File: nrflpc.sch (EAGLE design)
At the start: 68 parts, among them IC1 LPC1111/12/13/14-HVQFN33, IC2 LT1763CS8-3.3, IC3 LM3401, IC5 LM3401, IC6 LM3401, IC7 LM3401, Q1 20MHz, Q2 MOSFET-PCHANNEL, Q3 MOSFET-PCHANNEL, Q4 MOSFET-PCHANNEL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

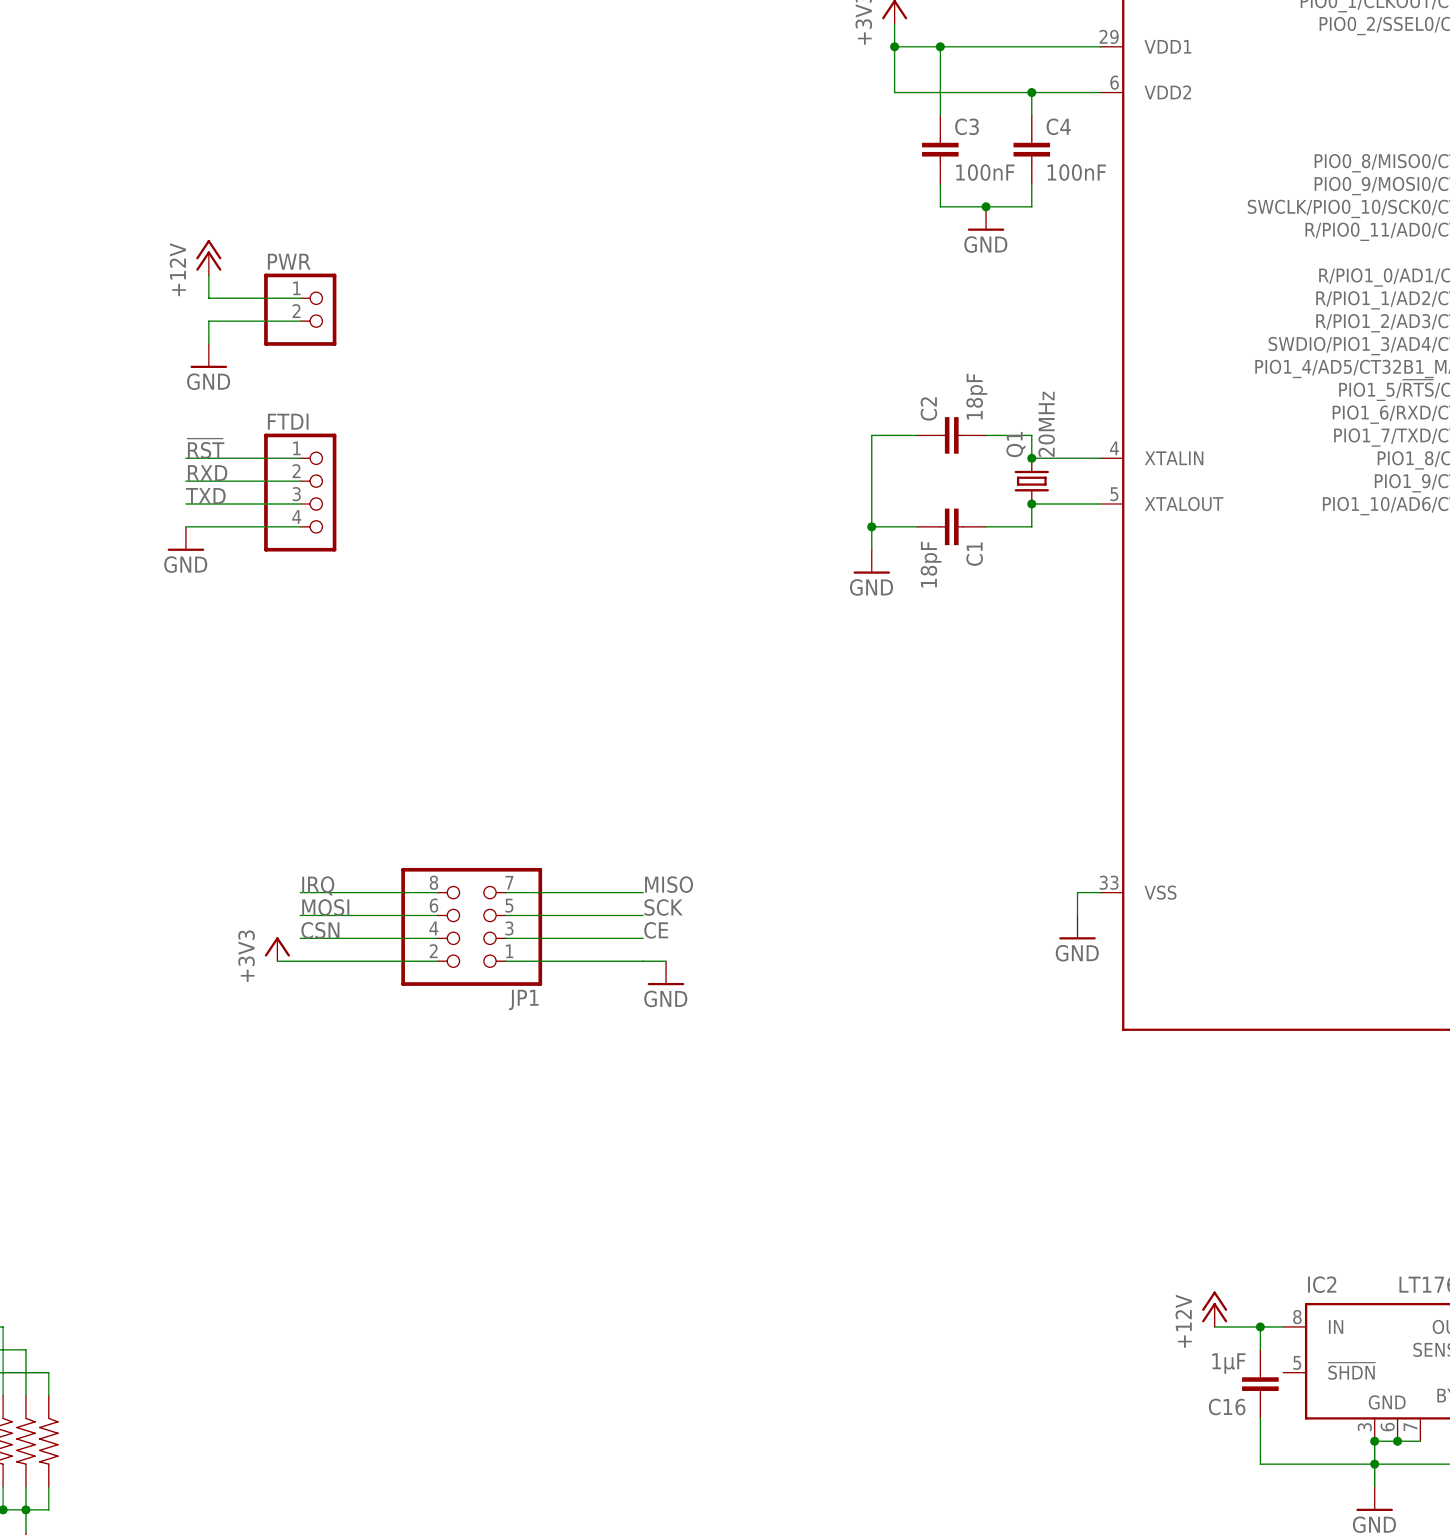
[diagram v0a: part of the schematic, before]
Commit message: Routing Voltage and "left" side (ISP)
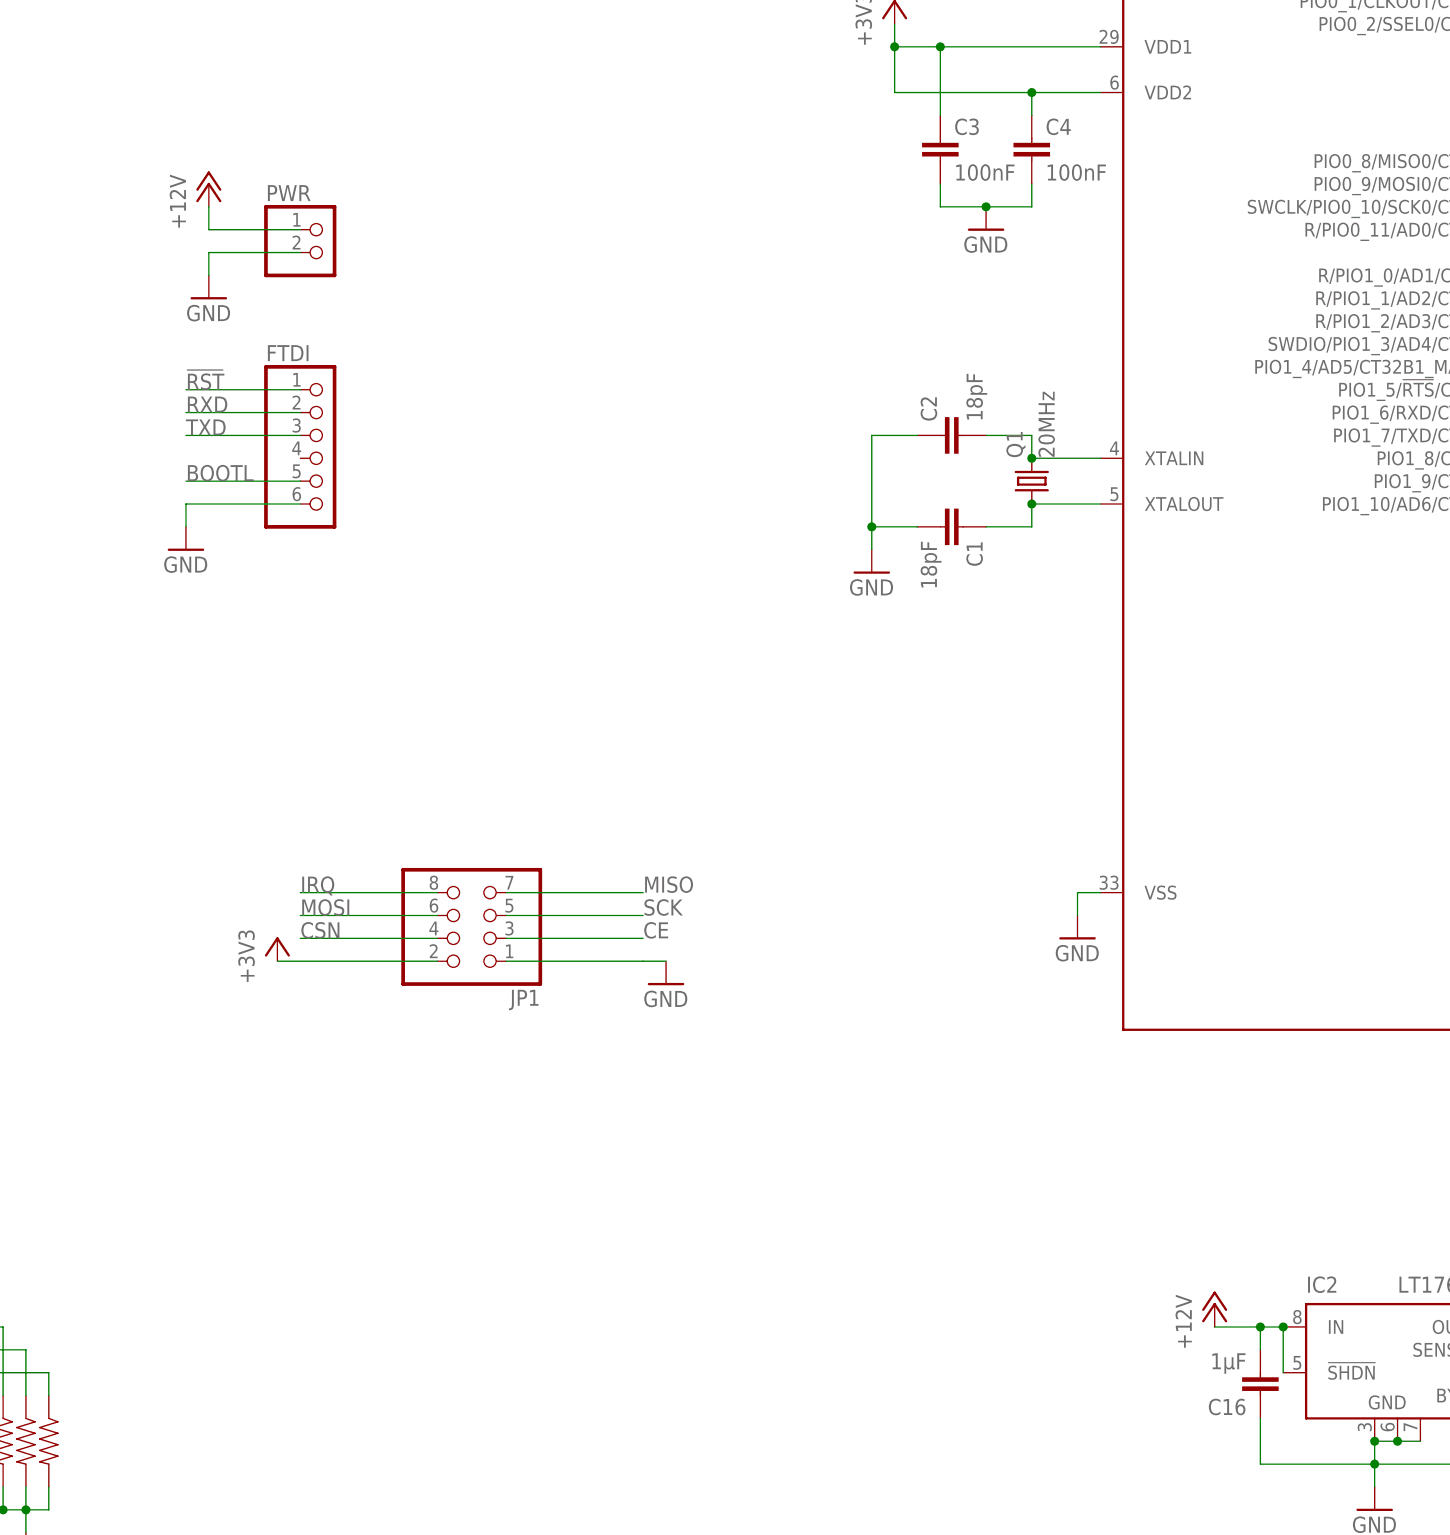
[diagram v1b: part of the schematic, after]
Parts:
- FTDI: device pinhead:PINHD-1X4 -> pinhead:PINHD-1X6
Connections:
- net +12V: now also IC2.!SHDN
- net BOOTL: now also FTDI.5
- net GND: now also FTDI.6; no longer FTDI.4
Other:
- moved on the sheet: PWR
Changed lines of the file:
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@@
 <part name="C16" library="SparkFun" deviceset="CAP" device="0805" value="1µF"/>
 <part name="+3V1" library="supply1" deviceset="+3V3" device=""/>
-<part name="FTDI" library="pinhead" deviceset="PINHD-1X4" device=""/>
+<part name="FTDI" library="pinhead" deviceset="PINHD-1X6" device=""/>
 <part name="GND8" library="supply1" deviceset="GND" device=""/>
 <part name="JP1" library="pinhead" deviceset="PINHD-2X4" device=""/>
@@
 <instance part="C16" gate="G$1" x="193.04" y="43.18" rot="R180"/>
 <instance part="+3V1" gate="G$1" x="243.84" y="50.8"/>
-<instance part="FTDI" gate="A" x="88.9" y="139.7"/>
+<instance part="FTDI" gate="A" x="88.9" y="144.78"/>
 <instance part="GND8" gate="1" x="73.66" y="134.62"/>
 <instance part="JP1" gate="A" x="106.68" y="93.98" rot="R180"/>
@@
 <instance part="GND13" gate="1" x="302.26" y="134.62"/>
 <instance part="C5" gate="G$1" x="302.26" y="144.78"/>
-<instance part="PWR" gate="G$1" x="88.9" y="160.02"/>
-<instance part="P+1" gate="1" x="76.2" y="167.64"/>
-<instance part="GND12" gate="1" x="76.2" y="154.94"/>
+<instance part="PWR" gate="G$1" x="88.9" y="167.64"/>
+<instance part="P+1" gate="1" x="76.2" y="175.26"/>
+<instance part="GND12" gate="1" x="76.2" y="162.56"/>
 <instance part="C12" gate="G$1" x="312.42" y="101.6" rot="R180"/>
 <instance part="R18" gate="G$1" x="322.58" y="109.22" rot="R180"/>
@@
 </segment>
 <segment>
-<pinref part="FTDI" gate="A" pin="4"/>
-<wire x1="86.36" y1="137.16" x2="73.66" y2="137.16" width="0.1524" layer="91"/>
-<pinref part="GND8" gate="1" pin="GND"/>
-</segment>
-<segment>
 <pinref part="JP1" gate="A" pin="1"/>
 <wire x1="109.22" y1="88.9" x2="124.46" y2="88.9" width="0.1524" layer="91"/>
@@
 <segment>
 <pinref part="PWR" gate="G$1" pin="2"/>
-<wire x1="86.36" y1="160.02" x2="76.2" y2="160.02" width="0.1524" layer="91"/>
-<wire x1="76.2" y1="160.02" x2="76.2" y2="157.48" width="0.1524" layer="91"/>
+<wire x1="86.36" y1="167.64" x2="76.2" y2="167.64" width="0.1524" layer="91"/>
+<wire x1="76.2" y1="167.64" x2="76.2" y2="165.1" width="0.1524" layer="91"/>
 <pinref part="GND12" gate="1" pin="GND"/>
 </segment>
@@
 <pinref part="GND15" gate="1" pin="GND"/>
 </segment>
+<segment>
+<pinref part="FTDI" gate="A" pin="6"/>
+<pinref part="GND8" gate="1" pin="GND"/>
+<wire x1="86.36" y1="139.7" x2="73.66" y2="139.7" width="0.1524" layer="91"/>
+<wire x1="73.66" y1="139.7" x2="73.66" y2="137.16" width="0.1524" layer="91"/>
+</segment>
 </net>
 <net name="!RST" class="0">
-<segment>
-<pinref part="FTDI" gate="A" pin="1"/>
-<wire x1="86.36" y1="144.78" x2="76.2" y2="144.78" width="0.1524" layer="91"/>
-<wire x1="76.2" y1="144.78" x2="73.66" y2="144.78" width="0.1524" layer="91"/>
-<label x="73.66" y="144.78" size="1.778" layer="95"/>
-</segment>
 <segment>
 <pinref part="C5" gate="G$1" pin="1"/>
@@
 <label x="236.22" y="198.12" size="1.778" layer="95"/>
 </segment>
+<segment>
+<pinref part="FTDI" gate="A" pin="1"/>
+<wire x1="86.36" y1="152.4" x2="73.66" y2="152.4" width="0.1524" layer="91"/>
+<label x="73.66" y="152.4" size="1.778" layer="95"/>
+</segment>
 </net>
 <net name="TXD" class="0">
-<segment>
-<pinref part="FTDI" gate="A" pin="3"/>
-<wire x1="86.36" y1="139.7" x2="73.66" y2="139.7" width="0.1524" layer="91"/>
-<label x="73.66" y="139.7" size="1.778" layer="95"/>
-</segment>
 <segment>
 <pinref part="R21" gate="G$1" pin="2"/>
@@
 <label x="248.92" y="147.32" size="1.778" layer="95"/>
 </segment>
+<segment>
+<pinref part="FTDI" gate="A" pin="3"/>
+<wire x1="86.36" y1="147.32" x2="73.66" y2="147.32" width="0.1524" layer="91"/>
+<label x="73.66" y="147.32" size="1.778" layer="95"/>
+</segment>
 </net>
 <net name="RXD" class="0">
-<segment>
-<pinref part="FTDI" gate="A" pin="2"/>
-<wire x1="86.36" y1="142.24" x2="73.66" y2="142.24" width="0.1524" layer="91"/>
-<label x="73.66" y="142.24" size="1.778" layer="95"/>
-</segment>
 <segment>
 <pinref part="R20" gate="G$1" pin="2"/>
 <wire x1="243.84" y1="149.86" x2="254" y2="149.86" width="0.1524" layer="91"/>
 <label x="248.92" y="149.86" size="1.778" layer="95"/>
+</segment>
+<segment>
+<pinref part="FTDI" gate="A" pin="2"/>
+<wire x1="86.36" y1="149.86" x2="73.66" y2="149.86" width="0.1524" layer="91"/>
+<label x="73.66" y="149.86" size="1.778" layer="95"/>
 </segment>
 </net>
@@
 <segment>
 <pinref part="PWR" gate="G$1" pin="1"/>
-<wire x1="86.36" y1="162.56" x2="76.2" y2="162.56" width="0.1524" layer="91"/>
-<wire x1="76.2" y1="162.56" x2="76.2" y2="165.1" width="0.1524" layer="91"/>
+<wire x1="86.36" y1="170.18" x2="76.2" y2="170.18" width="0.1524" layer="91"/>
+<wire x1="76.2" y1="170.18" x2="76.2" y2="172.72" width="0.1524" layer="91"/>
 <pinref part="P+1" gate="1" pin="+12V"/>
 </segment>
@@
 <wire x1="193.04" y1="45.72" x2="193.04" y2="48.26" width="0.1524" layer="91"/>
 <junction x="193.04" y="48.26"/>
+<pinref part="IC2" gate="G$1" pin="!SHDN"/>
+<wire x1="195.58" y1="43.18" x2="195.58" y2="48.26" width="0.1524" layer="91"/>
+<junction x="195.58" y="48.26"/>
 </segment>
 </net>
@@
 <wire x1="231.14" y1="195.58" x2="241.3" y2="195.58" width="0.1524" layer="91"/>
 </segment>
-</net>
+<segment>
+<pinref part="FTDI" gate="A" pin="5"/>
+<wire x1="86.36" y1="142.24" x2="73.66" y2="142.24" width="0.1524" layer="91"/>
+<label x="73.66" y="142.24" size="1.778" layer="95"/>
+</segment>
+</net>

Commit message: Almost final routing
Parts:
- added EXT: (no value), pinhead:PINHD-1X7
- added R1, R22: 1k, rcl:R-US_R0402
- added R23, R24, R25: 150, rcl:R-US_R0402
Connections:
- new net N$34: IC1.PIO0_3, R23.1
- new net N$35: IC1.PIO0_4/SCL, R24.1
- new net N$36: IC1.PIO0_5/SDA, R25.1
- net +3V3: now also EXT.6, R1.1, R22.1
- net AIN0: now also EXT.1, R1.2
- net AIN1: now also EXT.2, R22.2
- net GND: now also EXT.7
- net IO0: now also EXT.5, R23.2; no longer IC1.PIO0_3
- net IO1: now also EXT.4, R24.2; no longer IC1.PIO0_4/SCL
- net IO2: now also EXT.3, R25.2; no longer IC1.PIO0_5/SDA
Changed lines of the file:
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@@
 <part name="C18" library="SparkFun" deviceset="CAP" device="0402-CAP" value="10nF"/>
 <part name="C17" library="rcl" deviceset="CPOL-EU" device="SMCA" value="10µF"/>
+<part name="EXT" library="pinhead" deviceset="PINHD-1X7" device=""/>
+<part name="GND16" library="supply1" deviceset="GND" device=""/>
+<part name="+3V3" library="supply1" deviceset="+3V3" device=""/>
+<part name="R1" library="rcl" deviceset="R-US_" device="R0402" value="1k"/>
+<part name="R22" library="rcl" deviceset="R-US_" device="R0402" value="1k"/>
+<part name="+3V5" library="supply1" deviceset="+3V3" device=""/>
+<part name="+3V6" library="supply1" deviceset="+3V3" device=""/>
+<part name="R23" library="rcl" deviceset="R-US_" device="R0402" value="150"/>
+<part name="R24" library="rcl" deviceset="R-US_" device="R0402" value="150"/>
+<part name="R25" library="rcl" deviceset="R-US_" device="R0402" value="150"/>
 </parts>
 <sheets>
@@
 <instance part="C18" gate="G$1" x="228.6" y="43.18" rot="R180"/>
 <instance part="C17" gate="G$1" x="238.76" y="43.18"/>
+<instance part="EXT" gate="A" x="302.26" y="177.8"/>
+<instance part="GND16" gate="1" x="281.94" y="167.64"/>
+<instance part="+3V3" gate="G$1" x="281.94" y="175.26"/>
+<instance part="R1" gate="G$1" x="284.48" y="193.04" rot="R270"/>
+<instance part="R22" gate="G$1" x="276.86" y="193.04" rot="R270"/>
+<instance part="+3V5" gate="G$1" x="276.86" y="203.2"/>
+<instance part="+3V6" gate="G$1" x="284.48" y="203.2"/>
+<instance part="R23" gate="G$1" x="246.38" y="190.5"/>
+<instance part="R24" gate="G$1" x="246.38" y="187.96"/>
+<instance part="R25" gate="G$1" x="246.38" y="185.42"/>
 </instances>
 <busses>
@@
 <wire x1="73.66" y1="139.7" x2="73.66" y2="137.16" width="0.1524" layer="91"/>
 </segment>
+<segment>
+<pinref part="EXT" gate="A" pin="7"/>
+<wire x1="281.94" y1="170.18" x2="299.72" y2="170.18" width="0.1524" layer="91"/>
+<pinref part="GND16" gate="1" pin="GND"/>
+</segment>
 </net>
 <net name="!RST" class="0">
@@
 <junction x="167.64" y="185.42"/>
 </segment>
+<segment>
+<pinref part="EXT" gate="A" pin="6"/>
+<wire x1="281.94" y1="172.72" x2="299.72" y2="172.72" width="0.1524" layer="91"/>
+<pinref part="+3V3" gate="G$1" pin="+3V3"/>
+</segment>
+<segment>
+<pinref part="R22" gate="G$1" pin="1"/>
+<pinref part="+3V5" gate="G$1" pin="+3V3"/>
+<wire x1="276.86" y1="200.66" x2="276.86" y2="198.12" width="0.1524" layer="91"/>
+</segment>
+<segment>
+<pinref part="R1" gate="G$1" pin="1"/>
+<pinref part="+3V6" gate="G$1" pin="+3V3"/>
+<wire x1="284.48" y1="198.12" x2="284.48" y2="200.66" width="0.1524" layer="91"/>
+</segment>
 </net>
 <net name="CE" class="0">
@@
 <net name="IO0" class="0">
 <segment>
-<pinref part="IC1" gate="G$1" pin="PIO0_3"/>
-<wire x1="231.14" y1="190.5" x2="241.3" y2="190.5" width="0.1524" layer="91"/>
-<label x="236.22" y="190.5" size="1.778" layer="95"/>
+<pinref part="EXT" gate="A" pin="5"/>
+<wire x1="287.02" y1="175.26" x2="299.72" y2="175.26" width="0.1524" layer="91"/>
+<label x="287.02" y="175.26" size="1.778" layer="95"/>
+</segment>
+<segment>
+<pinref part="R23" gate="G$1" pin="2"/>
+<wire x1="251.46" y1="190.5" x2="259.08" y2="190.5" width="0.1524" layer="91"/>
+<label x="254" y="190.5" size="1.778" layer="95"/>
 </segment>
 </net>
 <net name="IO1" class="0">
 <segment>
-<pinref part="IC1" gate="G$1" pin="PIO0_4/SCL"/>
-<wire x1="231.14" y1="187.96" x2="241.3" y2="187.96" width="0.1524" layer="91"/>
-<label x="236.22" y="187.96" size="1.778" layer="95"/>
+<pinref part="EXT" gate="A" pin="4"/>
+<wire x1="299.72" y1="177.8" x2="287.02" y2="177.8" width="0.1524" layer="91"/>
+<label x="287.02" y="177.8" size="1.778" layer="95"/>
+</segment>
+<segment>
+<pinref part="R24" gate="G$1" pin="2"/>
+<wire x1="251.46" y1="187.96" x2="259.08" y2="187.96" width="0.1524" layer="91"/>
+<label x="254" y="187.96" size="1.778" layer="95"/>
 </segment>
 </net>
 <net name="IO2" class="0">
 <segment>
-<pinref part="IC1" gate="G$1" pin="PIO0_5/SDA"/>
-<wire x1="231.14" y1="185.42" x2="241.3" y2="185.42" width="0.1524" layer="91"/>
-<label x="236.22" y="185.42" size="1.778" layer="95"/>
+<pinref part="EXT" gate="A" pin="3"/>
+<wire x1="299.72" y1="180.34" x2="287.02" y2="180.34" width="0.1524" layer="91"/>
+<label x="287.02" y="180.34" size="1.778" layer="95"/>
+</segment>
+<segment>
+<pinref part="R25" gate="G$1" pin="2"/>
+<wire x1="251.46" y1="185.42" x2="259.08" y2="185.42" width="0.1524" layer="91"/>
+<label x="254" y="185.42" size="1.778" layer="95"/>
 </segment>
 </net>
@@
 <label x="330.2" y="109.22" size="1.778" layer="95"/>
 </segment>
+<segment>
+<pinref part="EXT" gate="A" pin="1"/>
+<wire x1="299.72" y1="185.42" x2="287.02" y2="185.42" width="0.1524" layer="91"/>
+<label x="287.02" y="185.42" size="1.778" layer="95"/>
+<pinref part="R1" gate="G$1" pin="2"/>
+<wire x1="287.02" y1="185.42" x2="284.48" y2="185.42" width="0.1524" layer="91"/>
+<wire x1="284.48" y1="185.42" x2="284.48" y2="187.96" width="0.1524" layer="91"/>
+</segment>
 </net>
 <net name="AIN1" class="0">
@@
 <wire x1="381" y1="109.22" x2="391.16" y2="109.22" width="0.1524" layer="91"/>
 <label x="383.54" y="109.22" size="1.778" layer="95"/>
+</segment>
+<segment>
+<pinref part="EXT" gate="A" pin="2"/>
+<wire x1="299.72" y1="182.88" x2="287.02" y2="182.88" width="0.1524" layer="91"/>
+<label x="287.02" y="182.88" size="1.778" layer="95"/>
+<pinref part="R22" gate="G$1" pin="2"/>
+<wire x1="287.02" y1="182.88" x2="276.86" y2="182.88" width="0.1524" layer="91"/>
+<wire x1="276.86" y1="182.88" x2="276.86" y2="187.96" width="0.1524" layer="91"/>
 </segment>
 </net>
@@
 </segment>
 </net>
+<net name="N$34" class="0">
+<segment>
+<pinref part="IC1" gate="G$1" pin="PIO0_3"/>
+<pinref part="R23" gate="G$1" pin="1"/>
+<wire x1="231.14" y1="190.5" x2="241.3" y2="190.5" width="0.1524" layer="91"/>
+</segment>
+</net>
+<net name="N$35" class="0">
+<segment>
+<pinref part="R24" gate="G$1" pin="1"/>
+<pinref part="IC1" gate="G$1" pin="PIO0_4/SCL"/>
+<wire x1="241.3" y1="187.96" x2="231.14" y2="187.96" width="0.1524" layer="91"/>
+</segment>
+</net>
+<net name="N$36" class="0">
+<segment>
+<pinref part="IC1" gate="G$1" pin="PIO0_5/SDA"/>
+<pinref part="R25" gate="G$1" pin="1"/>
+<wire x1="231.14" y1="185.42" x2="241.3" y2="185.42" width="0.1524" layer="91"/>
+</segment>
+</net>
